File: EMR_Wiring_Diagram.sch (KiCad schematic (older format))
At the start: 1 part

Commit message: Renamed Part library
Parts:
- removed U?: EMDrive_500, symbol EMDrive_500
- added U?: EMDrive_500, symbol EMDrive_500
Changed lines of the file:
@@
 EESchema Schematic File Version 2
+LIBS:EMR_Wiring_Diagram-rescue
 LIBS:power
 LIBS:device
@@
 LIBS:contrib
 LIBS:valves
-LIBS:emdrive_500
+LIBS:EMR_Parts
 LIBS:EMR_Wiring_Diagram-cache
 EELAYER 25 0
@@
 $Comp
 L EMDrive_500 U?
-U 1 1 56AACBB9
-P 2950 2850
-F 0 "U?" H 3000 3600 60  0001 C CNN
-F 1 "EMDrive_500" H 3000 3600 60  0000 C CNN
-F 2 "" H 3000 3600 60  0000 C CNN
-F 3 "" H 3000 3600 60  0000 C CNN
-	1    2950 2850
+U 1 1 56AFEA7B
+P 3000 3100
+F 0 "U?" H 3050 3850 60  0001 C CNN
+F 1 "EMDrive_500" H 3050 3850 60  0000 C CNN
+F 2 "" H 3050 3850 60  0000 C CNN
+F 3 "" H 3050 3850 60  0000 C CNN
+	1    3000 3100
 	1    0    0    -1
 $EndComp

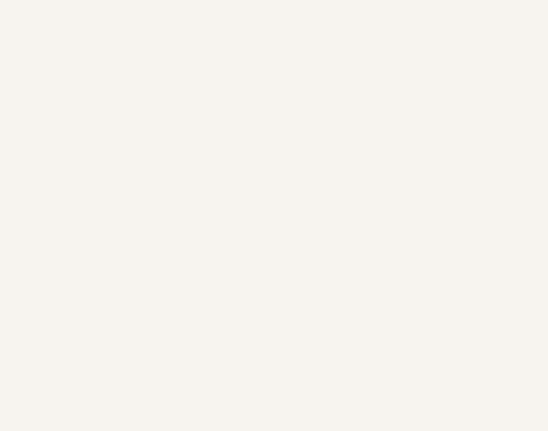
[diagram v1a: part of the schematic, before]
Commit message: Added motor
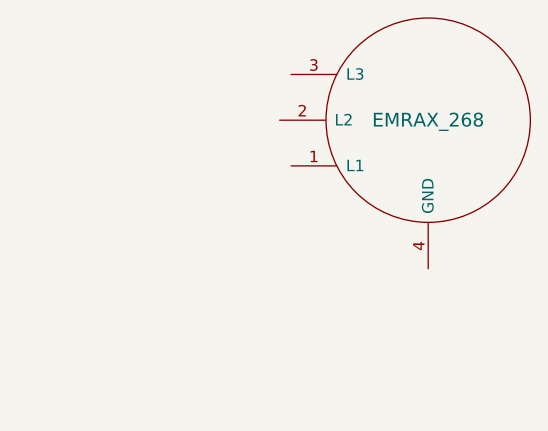
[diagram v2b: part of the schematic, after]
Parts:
- added U?: EMRAX_268, symbol EMRAX_268
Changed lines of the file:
@@
+	1    0    0    -1
+$EndComp
+$Comp
+L EMRAX_268 U?
+U 1 1 56AFEE2A
+P 6500 2400
+F 0 "U?" H 6500 2400 60  0001 C CNN
+F 1 "EMRAX_268" H 6500 2400 60  0000 C CNN
+F 2 "" H 6500 2400 60  0000 C CNN
+F 3 "" H 6500 2400 60  0000 C CNN
+	1    6500 2400
 	1    0    0    -1
 $EndComp

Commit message: Split motor and resolver into separate parts
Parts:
- removed U?: EMDrive_500, symbol EMDrive_500
- removed U?: EMRAX_268, symbol EMRAX_268
- added U?: EMDrive_500, symbol EMDrive_500
- added U?: EMRAX_268, symbol EMRAX_268
- added U?: EMRAX_268_Resolver, symbol EMRAX_268_Resolver
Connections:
- wire segments 0 -> 19
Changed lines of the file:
@@
 $Comp
 L EMDrive_500 U?
-U 1 1 56AFEA7B
-P 3000 3100
-F 0 "U?" H 3050 3850 60  0001 C CNN
-F 1 "EMDrive_500" H 3050 3850 60  0000 C CNN
-F 2 "" H 3050 3850 60  0000 C CNN
-F 3 "" H 3050 3850 60  0000 C CNN
-	1    3000 3100
+U 1 1 56B01C57
+P 5700 3200
+F 0 "U?" H 5750 3950 60  0001 C CNN
+F 1 "EMDrive_500" H 5750 3950 60  0000 C CNN
+F 2 "" H 5750 3950 60  0000 C CNN
+F 3 "" H 5750 3950 60  0000 C CNN
+	1    5700 3200
 	1    0    0    -1
 $EndComp
 $Comp
 L EMRAX_268 U?
-U 1 1 56AFEE2A
-P 6500 2400
-F 0 "U?" H 6500 2400 60  0001 C CNN
-F 1 "EMRAX_268" H 6500 2400 60  0000 C CNN
-F 2 "" H 6500 2400 60  0000 C CNN
-F 3 "" H 6500 2400 60  0000 C CNN
-	1    6500 2400
+U 1 1 56B01C6B
+P 3250 4000
+F 0 "U?" H 3250 4000 60  0001 C CNN
+F 1 "EMRAX_268" H 3250 4000 60  0000 C CNN
+F 2 "" H 3250 4000 60  0000 C CNN
+F 3 "" H 3250 4000 60  0000 C CNN
+	1    3250 4000
+	-1   0    0    -1
+$EndComp
+$Comp
+L EMRAX_268_Resolver U?
+U 1 1 56B01C7F
+P 8500 4400
+F 0 "U?" H 8500 4400 60  0001 C CNN
+F 1 "EMRAX_268_Resolver" H 8500 4400 60  0000 C CNN
+F 2 "" H 8500 4400 60  0000 C CNN
+F 3 "" H 8500 4400 60  0000 C CNN
+	1    8500 4400
 	1    0    0    -1
 $EndComp
+Wire Wire Line
+	3850 3800 4000 3800
+Wire Wire Line
+	4000 3800 4000 3900
+Wire Wire Line
+	4000 3900 4150 3900
+Wire Wire Line
+	3900 4000 4150 4000
+Wire Wire Line
+	3850 4200 4000 4200
+Wire Wire Line
+	4000 4200 4000 4100
+Wire Wire Line
+	4000 4100 4150 4100
+Wire Wire Line
+	7700 4600 7150 4600
+Wire Wire Line
+	7700 4700 7150 4700
+Wire Wire Line
+	7700 4800 7150 4800
+Wire Wire Line
+	7700 4900 7150 4900
+Wire Wire Line
+	7700 5000 7150 5000
+Wire Wire Line
+	7700 5100 7150 5100
+Wire Wire Line
+	7700 4250 7500 4250
+Wire Wire Line
+	7500 4250 7500 4000
+Wire Wire Line
+	7500 4000 7150 4000
+Wire Wire Line
+	7700 4350 7400 4350
+Wire Wire Line
+	7400 4350 7400 4100
+Wire Wire Line
+	7400 4100 7150 4100
 $EndSCHEMATC

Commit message: Added ignition and emergency stop
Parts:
- added 4A, 800A: FUSE, symbol FUSE
- added Precharge: 50, symbol R
- added SW1: Emergency Switch, symbol SW_PUSH
- added SW?: Ignition Key, symbol SPST
- added U?: Battery_Pack, symbol Battery_Pack
- added U?: Line_contactor, symbol Line_contactor
- U?: symbol EMDrive_500 -> EMDrive_500-RESCUE-EMR_Wiring_Diagram
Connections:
- net labels added: +12V
- wire segments 19 -> 41
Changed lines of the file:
@@
 $EndDescr
 $Comp
-L EMDrive_500 U?
+L EMDrive_500-RESCUE-EMR_Wiring_Diagram U?
 U 1 1 56B01C57
 P 5700 3200
@@
 	1    0    0    -1
 $EndComp
+$Comp
+L Battery_Pack U?
+U 1 1 56B0DD37
+P 10200 1600
+F 0 "U?" H 10200 1600 60  0001 C CNN
+F 1 "Battery_Pack" H 10200 1600 60  0000 C CNN
+F 2 "" H 10200 1600 60  0000 C CNN
+F 3 "" H 10200 1600 60  0000 C CNN
+	1    10200 1600
+	-1   0    0    -1
+$EndComp
 Wire Wire Line
 	3850 3800 4000 3800
@@
 Wire Wire Line
 	7400 4100 7150 4100
+$Comp
+L FUSE 4A
+U 1 1 56B0DEE6
+P 8850 1150
+F 0 "4A" H 8950 1200 50  0000 C CNN
+F 1 "FUSE" H 8750 1100 50  0000 C CNN
+F 2 "" H 8850 1150 50  0000 C CNN
+F 3 "" H 8850 1150 50  0000 C CNN
+	1    8850 1150
+	-1   0    0    -1
+$EndComp
+$Comp
+L SPST SW?
+U 1 1 56B0DF9A
+P 8000 1150
+F 0 "SW?" H 8000 1250 50  0000 C CNN
+F 1 "Ignition Key" H 8000 1050 50  0000 C CNN
+F 2 "" H 8000 1150 50  0000 C CNN
+F 3 "" H 8000 1150 50  0000 C CNN
+	1    8000 1150
+	-1   0    0    -1
+$EndComp
+Wire Wire Line
+	8600 1150 8500 1150
+Wire Wire Line
+	7400 1150 7400 1600
+$Comp
+L R Precharge
+U 1 1 56B0E1B1
+P 7850 2650
+F 0 "Precharge" V 7930 2650 50  0000 C CNN
+F 1 "50" V 7850 2650 50  0000 C CNN
+F 2 "" V 7780 2650 50  0000 C CNN
+F 3 "" H 7850 2650 50  0000 C CNN
+	1    7850 2650
+	1    0    0    1
+$EndComp
+Connection ~ 7400 1600
+Wire Wire Line
+	9000 1700 9000 3600
+Wire Wire Line
+	7150 1700 9450 1700
+Wire Wire Line
+	7150 1600 7850 1600
+$Comp
+L SW_PUSH SW1
+U 1 1 56B0ECDC
+P 7700 2100
+F 0 "SW1" H 7850 2210 50  0000 C CNN
+F 1 "Emergency Switch" H 7700 2020 50  0000 C CNN
+F 2 "" H 7700 2100 50  0000 C CNN
+F 3 "" H 7700 2100 50  0000 C CNN
+	1    7700 2100
+	0    -1   1    0
+$EndComp
+Wire Wire Line
+	7150 1800 7700 1800
+Wire Wire Line
+	7700 2400 7450 2400
+Wire Wire Line
+	7450 2400 7450 2200
+Wire Wire Line
+	7450 2200 7150 2200
+$Comp
+L FUSE 800A
+U 1 1 56B0EDB7
+P 9000 1500
+F 0 "800A" H 9100 1550 50  0000 C CNN
+F 1 "FUSE" H 8900 1450 50  0000 C CNN
+F 2 "" H 9000 1500 50  0000 C CNN
+F 3 "" H 9000 1500 50  0000 C CNN
+	1    9000 1500
+	-1   0    0    -1
+$EndComp
+Wire Wire Line
+	9000 3600 7150 3600
+$Comp
+L +12V #PWR?
+U 1 1 56B0EEB7
+P 8250 2050
+F 0 "#PWR?" H 8250 1900 50  0001 C CNN
+F 1 "+12V" H 8250 2190 50  0000 C CNN
+F 2 "" H 8250 2050 50  0000 C CNN
+F 3 "" H 8250 2050 50  0000 C CNN
+	1    8250 2050
+	1    0    0    -1
+$EndComp
+$Comp
+L Line_contactor U?
+U 1 1 56B0F345
+P 8650 3050
+F 0 "U?" H 9250 3600 60  0000 C CNN
+F 1 "Line_contactor" H 9250 3600 60  0000 C CNN
+F 2 "" H 9250 3600 60  0000 C CNN
+F 3 "" H 9250 3600 60  0000 C CNN
+	1    8650 3050
+	0    -1   -1   0
+$EndComp
+Wire Wire Line
+	7850 1600 7850 2500
+Wire Wire Line
+	7850 2800 7850 3500
+Connection ~ 7850 3500
+Wire Wire Line
+	7150 3000 8250 3000
+Wire Wire Line
+	7500 1150 7400 1150
+Connection ~ 9000 1700
+Wire Wire Line
+	9450 1500 9250 1500
+Wire Wire Line
+	9100 1150 9350 1150
+Wire Wire Line
+	9350 1150 9350 1500
+Connection ~ 9350 1500
+Wire Wire Line
+	8750 1500 8650 1500
+Wire Wire Line
+	8650 1500 8650 2050
+Wire Wire Line
+	8250 3000 8250 2850
+Wire Wire Line
+	7150 3500 8650 3500
+Wire Wire Line
+	8650 3500 8650 2850
 $EndSCHEMATC

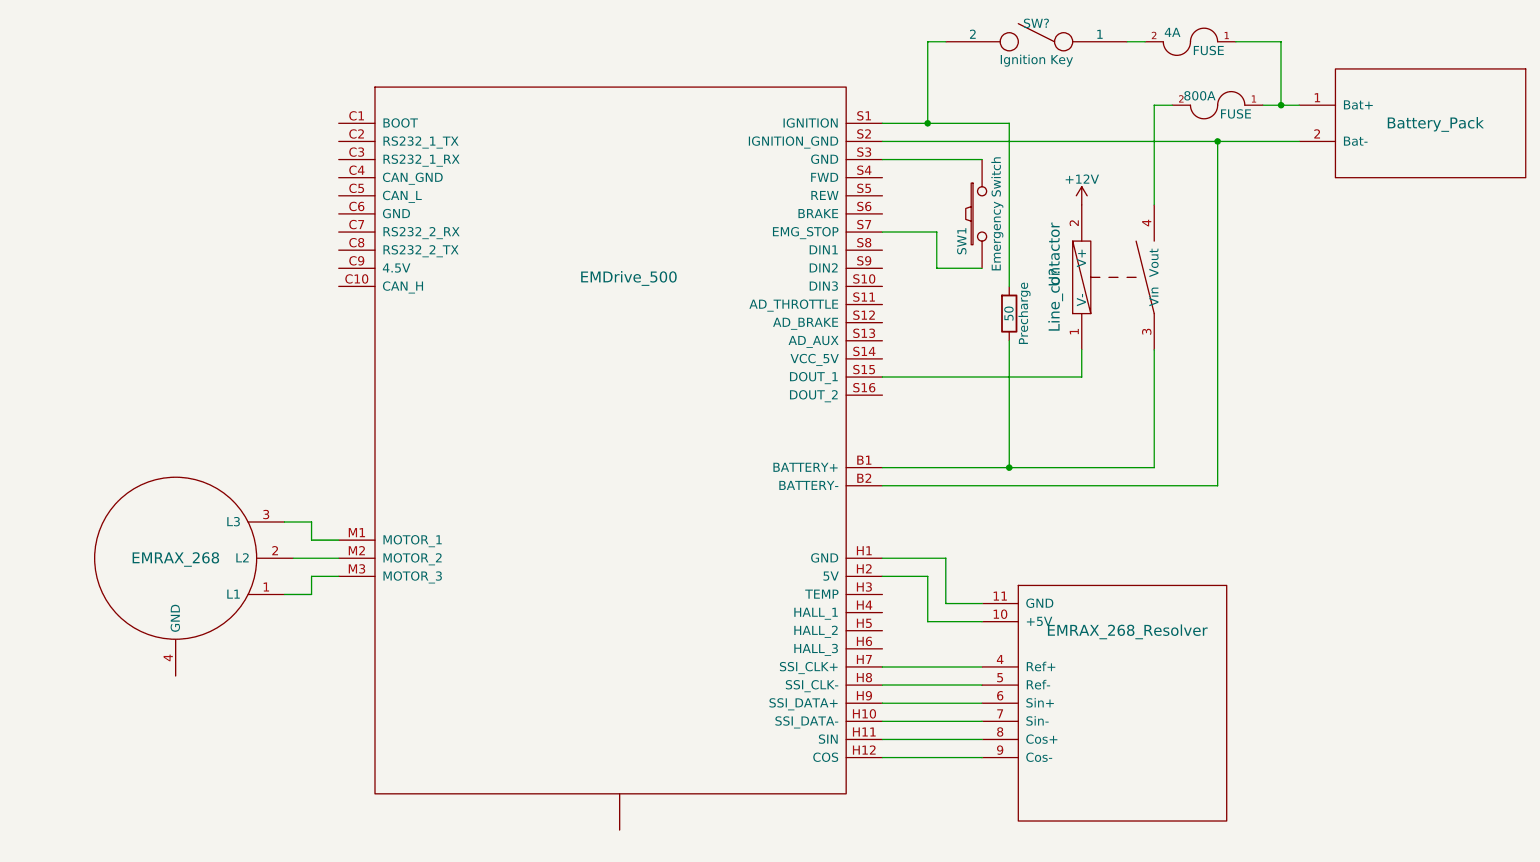
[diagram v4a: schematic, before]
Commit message: Fixed motor ground connection
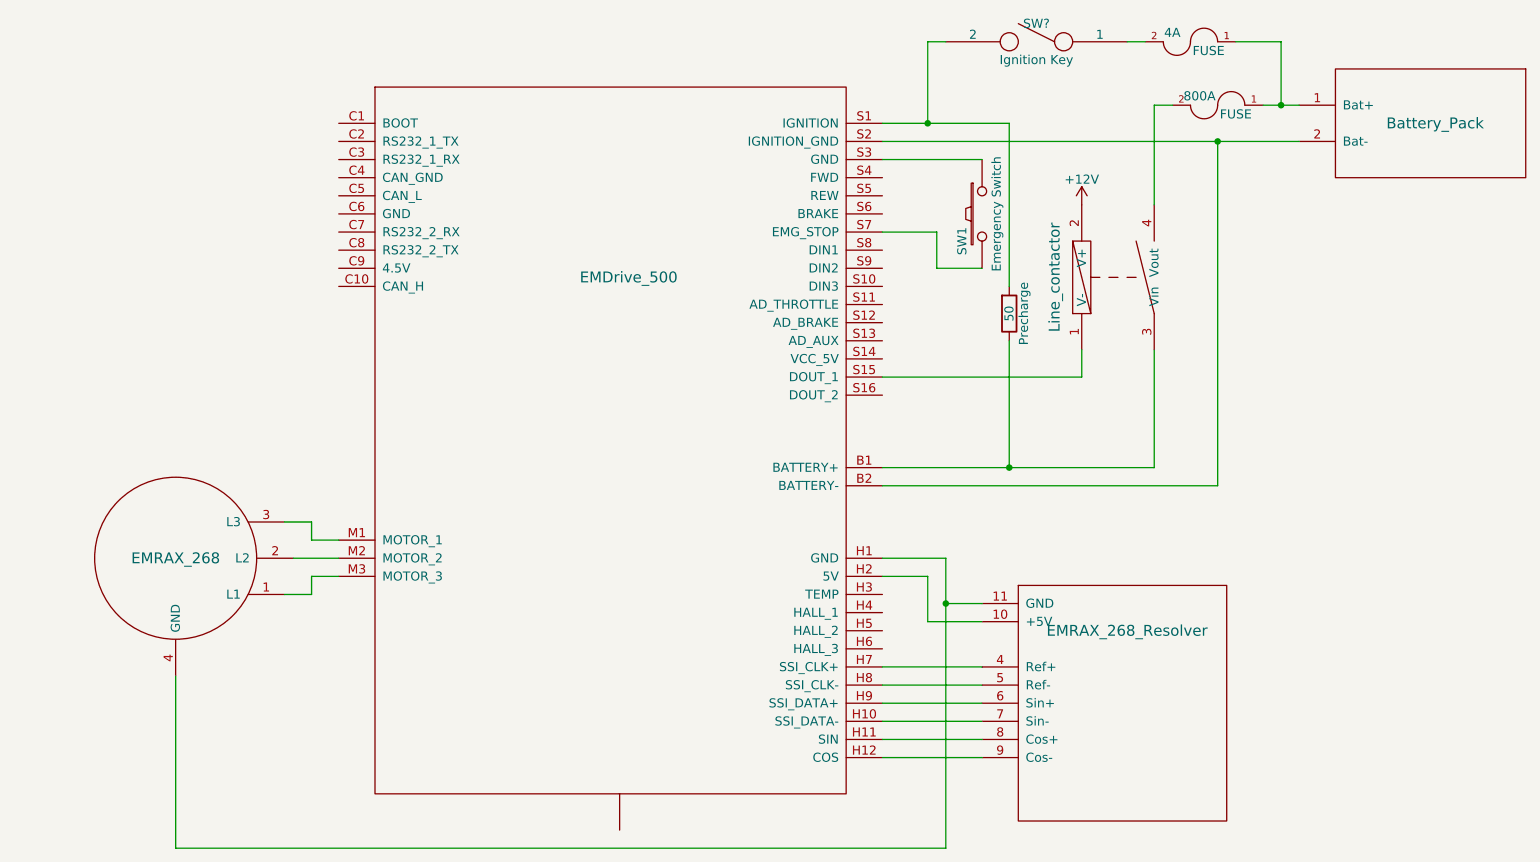
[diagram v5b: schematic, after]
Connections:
- net at U?.11 (GND), U?.H1 (GND): now also U?.4 (GND)
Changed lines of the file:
@@
 	-1   0    0    -1
+$EndComp
+$Comp
+L FUSE 4A
+U 1 1 56B0DEE6
+P 8850 1150
+F 0 "4A" H 8950 1200 50  0000 C CNN
+F 1 "FUSE" H 8750 1100 50  0000 C CNN
+F 2 "" H 8850 1150 50  0000 C CNN
+F 3 "" H 8850 1150 50  0000 C CNN
+	1    8850 1150
+	-1   0    0    -1
+$EndComp
+$Comp
+L SPST SW?
+U 1 1 56B0DF9A
+P 8000 1150
+F 0 "SW?" H 8000 1250 50  0000 C CNN
+F 1 "Ignition Key" H 8000 1050 50  0000 C CNN
+F 2 "" H 8000 1150 50  0000 C CNN
+F 3 "" H 8000 1150 50  0000 C CNN
+	1    8000 1150
+	-1   0    0    -1
+$EndComp
+$Comp
+L R Precharge
+U 1 1 56B0E1B1
+P 7850 2650
+F 0 "Precharge" V 7930 2650 50  0000 C CNN
+F 1 "50" V 7850 2650 50  0000 C CNN
+F 2 "" V 7780 2650 50  0000 C CNN
+F 3 "" H 7850 2650 50  0000 C CNN
+	1    7850 2650
+	1    0    0    1
+$EndComp
+$Comp
+L SW_PUSH SW1
+U 1 1 56B0ECDC
+P 7700 2100
+F 0 "SW1" H 7850 2210 50  0000 C CNN
+F 1 "Emergency Switch" H 7700 2020 50  0000 C CNN
+F 2 "" H 7700 2100 50  0000 C CNN
+F 3 "" H 7700 2100 50  0000 C CNN
+	1    7700 2100
+	0    -1   1    0
+$EndComp
+$Comp
+L FUSE 800A
+U 1 1 56B0EDB7
+P 9000 1500
+F 0 "800A" H 9100 1550 50  0000 C CNN
+F 1 "FUSE" H 8900 1450 50  0000 C CNN
+F 2 "" H 9000 1500 50  0000 C CNN
+F 3 "" H 9000 1500 50  0000 C CNN
+	1    9000 1500
+	-1   0    0    -1
+$EndComp
+$Comp
+L +12V #PWR?
+U 1 1 56B0EEB7
+P 8250 2050
+F 0 "#PWR?" H 8250 1900 50  0001 C CNN
+F 1 "+12V" H 8250 2190 50  0000 C CNN
+F 2 "" H 8250 2050 50  0000 C CNN
+F 3 "" H 8250 2050 50  0000 C CNN
+	1    8250 2050
+	1    0    0    -1
+$EndComp
+$Comp
+L Line_contactor U?
+U 1 1 56B0F345
+P 8650 3050
+F 0 "U?" H 9250 3600 60  0001 C CNN
+F 1 "Line_contactor" H 9250 3600 60  0000 C CNN
+F 2 "" H 9250 3600 60  0000 C CNN
+F 3 "" H 9250 3600 60  0000 C CNN
+	1    8650 3050
+	0    -1   -1   0
 $EndComp
 Wire Wire Line
@@
 	7700 4250 7500 4250
 Wire Wire Line
-	7500 4250 7500 4000
+	7500 4000 7500 5600
 Wire Wire Line
 	7500 4000 7150 4000
@@
 Wire Wire Line
 	7400 4100 7150 4100
-$Comp
-L FUSE 4A
-U 1 1 56B0DEE6
-P 8850 1150
-F 0 "4A" H 8950 1200 50  0000 C CNN
-F 1 "FUSE" H 8750 1100 50  0000 C CNN
-F 2 "" H 8850 1150 50  0000 C CNN
-F 3 "" H 8850 1150 50  0000 C CNN
-	1    8850 1150
-	-1   0    0    -1
-$EndComp
-$Comp
-L SPST SW?
-U 1 1 56B0DF9A
-P 8000 1150
-F 0 "SW?" H 8000 1250 50  0000 C CNN
-F 1 "Ignition Key" H 8000 1050 50  0000 C CNN
-F 2 "" H 8000 1150 50  0000 C CNN
-F 3 "" H 8000 1150 50  0000 C CNN
-	1    8000 1150
-	-1   0    0    -1
-$EndComp
 Wire Wire Line
 	8600 1150 8500 1150
 Wire Wire Line
 	7400 1150 7400 1600
-$Comp
-L R Precharge
-U 1 1 56B0E1B1
-P 7850 2650
-F 0 "Precharge" V 7930 2650 50  0000 C CNN
-F 1 "50" V 7850 2650 50  0000 C CNN
-F 2 "" V 7780 2650 50  0000 C CNN
-F 3 "" H 7850 2650 50  0000 C CNN
-	1    7850 2650
-	1    0    0    1
-$EndComp
 Connection ~ 7400 1600
 Wire Wire Line
@@
 Wire Wire Line
 	7150 1600 7850 1600
-$Comp
-L SW_PUSH SW1
-U 1 1 56B0ECDC
-P 7700 2100
-F 0 "SW1" H 7850 2210 50  0000 C CNN
-F 1 "Emergency Switch" H 7700 2020 50  0000 C CNN
-F 2 "" H 7700 2100 50  0000 C CNN
-F 3 "" H 7700 2100 50  0000 C CNN
-	1    7700 2100
-	0    -1   1    0
-$EndComp
 Wire Wire Line
 	7150 1800 7700 1800
@@
 Wire Wire Line
 	7450 2200 7150 2200
-$Comp
-L FUSE 800A
-U 1 1 56B0EDB7
-P 9000 1500
-F 0 "800A" H 9100 1550 50  0000 C CNN
-F 1 "FUSE" H 8900 1450 50  0000 C CNN
-F 2 "" H 9000 1500 50  0000 C CNN
-F 3 "" H 9000 1500 50  0000 C CNN
-	1    9000 1500
-	-1   0    0    -1
-$EndComp
 Wire Wire Line
 	9000 3600 7150 3600
-$Comp
-L +12V #PWR?
-U 1 1 56B0EEB7
-P 8250 2050
-F 0 "#PWR?" H 8250 1900 50  0001 C CNN
-F 1 "+12V" H 8250 2190 50  0000 C CNN
-F 2 "" H 8250 2050 50  0000 C CNN
-F 3 "" H 8250 2050 50  0000 C CNN
-	1    8250 2050
-	1    0    0    -1
-$EndComp
-$Comp
-L Line_contactor U?
-U 1 1 56B0F345
-P 8650 3050
-F 0 "U?" H 9250 3600 60  0000 C CNN
-F 1 "Line_contactor" H 9250 3600 60  0000 C CNN
-F 2 "" H 9250 3600 60  0000 C CNN
-F 3 "" H 9250 3600 60  0000 C CNN
-	1    8650 3050
-	0    -1   -1   0
-$EndComp
 Wire Wire Line
 	7850 1600 7850 2500
@@
 Wire Wire Line
 	8650 3500 8650 2850
+Wire Wire Line
+	7500 5600 3250 5600
+Wire Wire Line
+	3250 5600 3250 4650
+Connection ~ 7500 4250
 $EndSCHEMATC

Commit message: Added earth ground to motor and controller
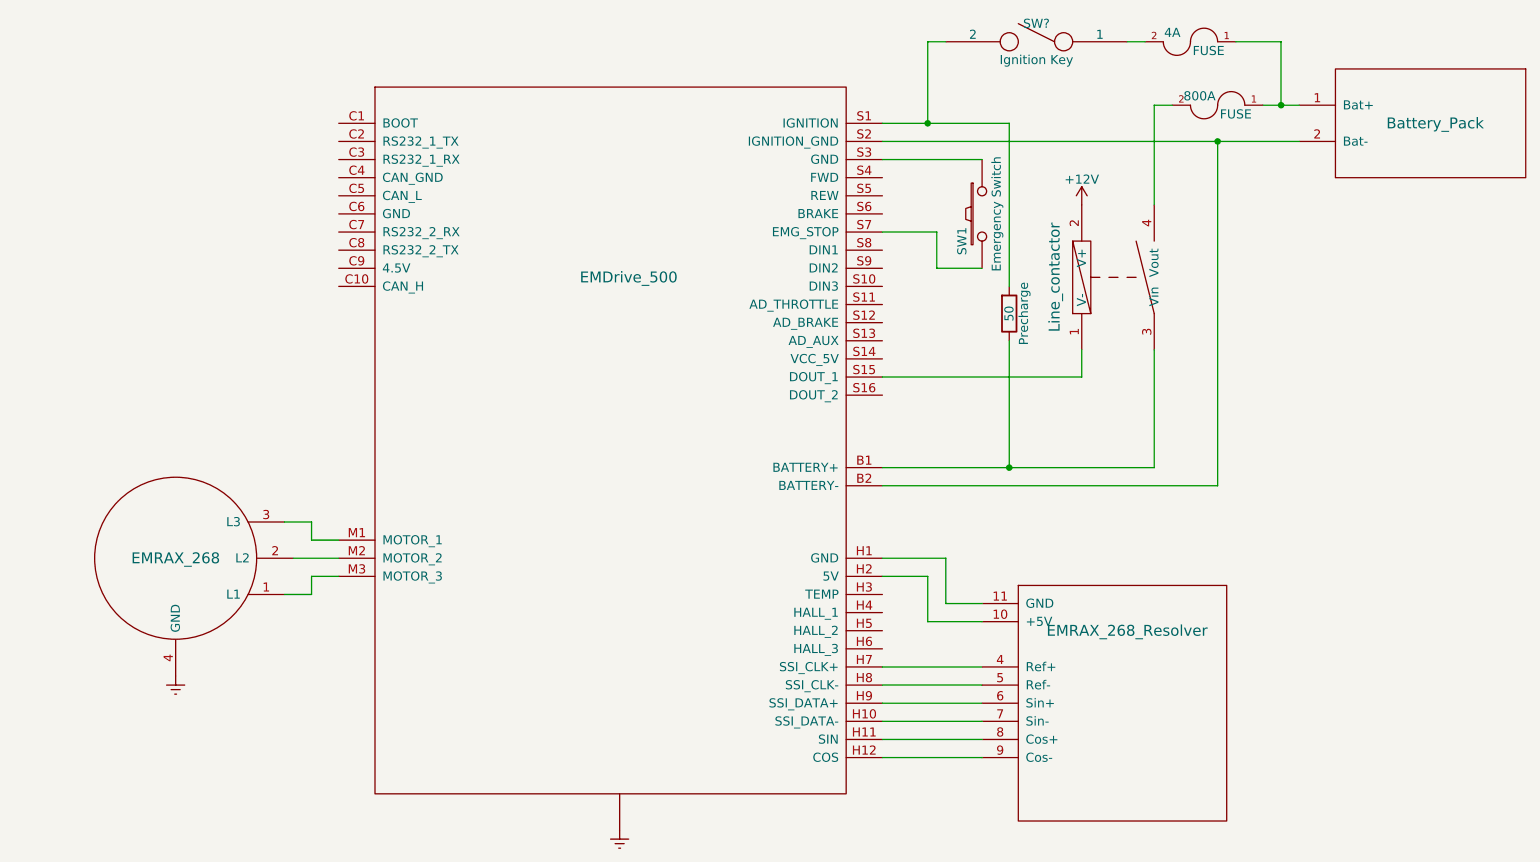
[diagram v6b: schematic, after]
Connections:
- net at U?.11 (GND), U?.H1 (GND): no longer U?.4 (GND)
- net Earth: now reaches U?.~
- net Earth: now also U?.4 (GND)
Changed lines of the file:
@@
 	0    -1   -1   0
+$EndComp
+$Comp
+L Earth #PWR?
+U 1 1 56B15939
+P 3250 4650
+F 0 "#PWR?" H 3250 4400 50  0001 C CNN
+F 1 "Earth" H 3250 4500 50  0001 C CNN
+F 2 "" H 3250 4650 50  0000 C CNN
+F 3 "" H 3250 4650 50  0000 C CNN
+	1    3250 4650
+	1    0    0    -1
 $EndComp
 Wire Wire Line
@@
 Wire Wire Line
 	7700 4250 7500 4250
-Wire Wire Line
-	7500 4000 7500 5600
-Wire Wire Line
-	7500 4000 7150 4000
 Wire Wire Line
 	7700 4350 7400 4350
@@
 Connection ~ 9000 1700
 Wire Wire Line
-	9450 1500 9250 1500
+	9250 1500 9450 1500
 Wire Wire Line
 	9100 1150 9350 1150
@@
 	8650 3500 8650 2850
 Wire Wire Line
-	7500 5600 3250 5600
+	7150 4000 7500 4000
 Wire Wire Line
-	3250 5600 3250 4650
-Connection ~ 7500 4250
+	7500 4000 7500 4250
+$Comp
+L Earth #PWR?
+U 1 1 56B16319
+P 5700 5500
+F 0 "#PWR?" H 5700 5250 50  0001 C CNN
+F 1 "Earth" H 5700 5350 50  0001 C CNN
+F 2 "" H 5700 5500 50  0000 C CNN
+F 3 "" H 5700 5500 50  0000 C CNN
+	1    5700 5500
+	1    0    0    -1
+$EndComp
 $EndSCHEMATC

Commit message: component names
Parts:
- gave numbers to parts that had none: 1
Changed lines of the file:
@@
 $EndComp
 $Comp
-L SPST SW?
+L SPST SW2
 U 1 1 56B0DF9A
 P 8000 1150
-F 0 "SW?" H 8000 1250 50  0000 C CNN
+F 0 "SW2" H 8000 1250 50  0000 C CNN
 F 1 "Ignition Key" H 8000 1050 50  0000 C CNN
 F 2 "" H 8000 1150 50  0000 C CNN
